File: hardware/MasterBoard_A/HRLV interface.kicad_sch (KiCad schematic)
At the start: 27 parts, among them Q10 MMBT5550L, Q11 MMBT5550L, Q3 MMBT5550L, U30 MCP2542FDxMF, U31 STISO620, U32 STISO620

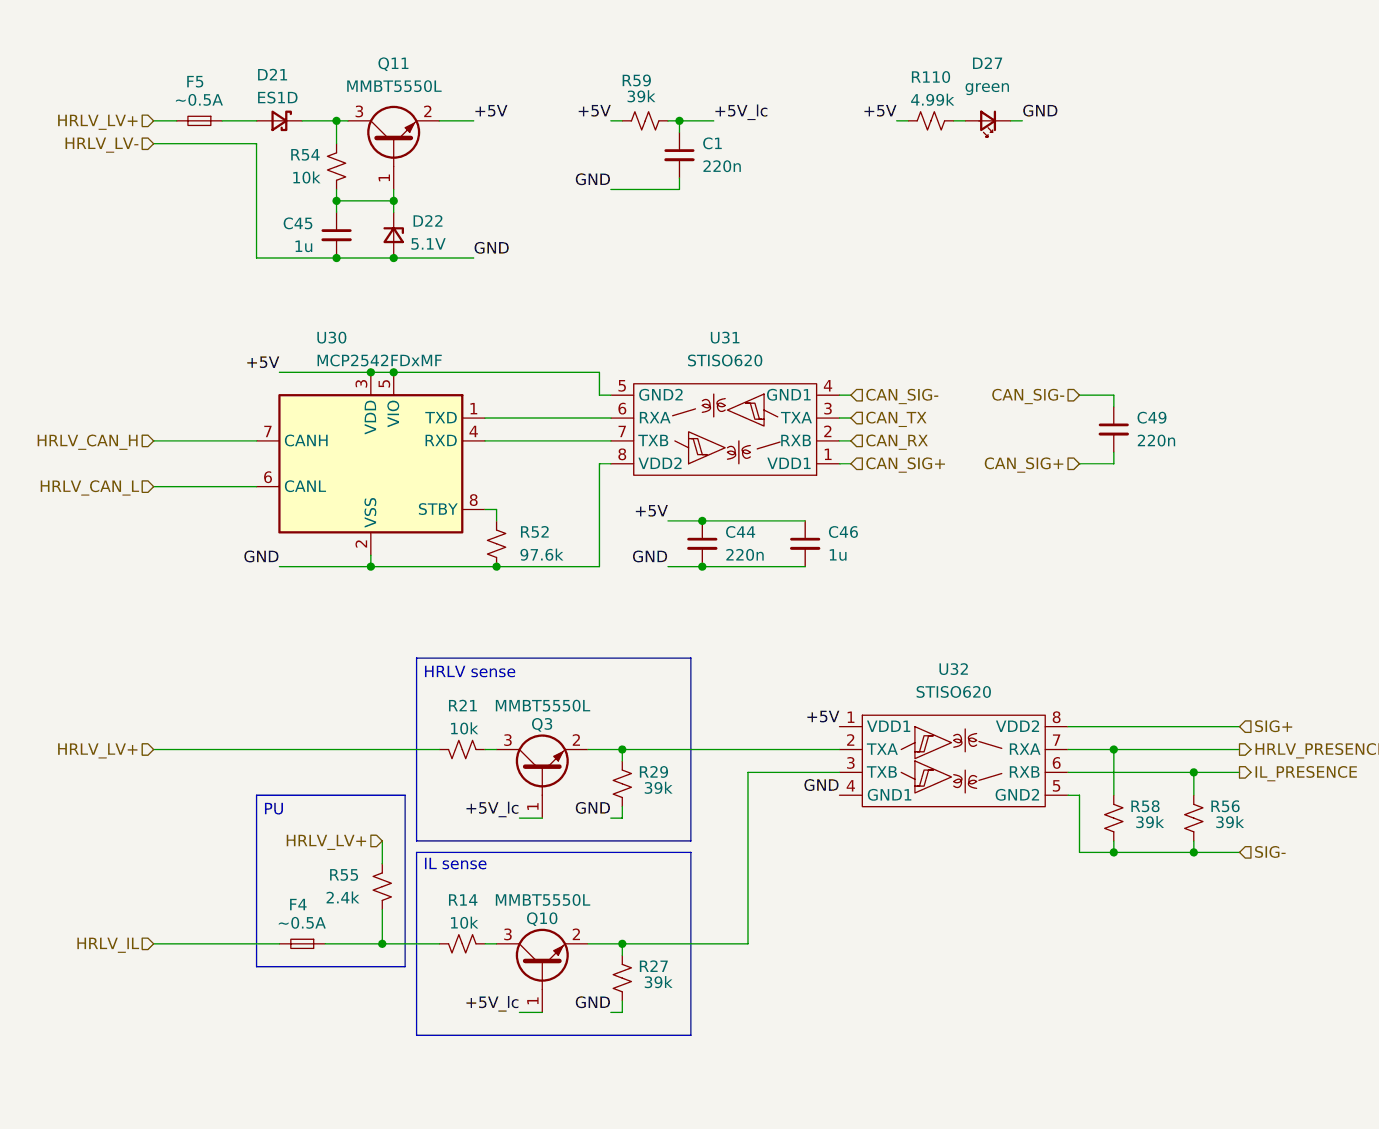
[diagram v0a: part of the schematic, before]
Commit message: better-ified power stuff. new costing program
handy new costing program for kicad. just c&p symbols directly from kicad into it and itll dump out the BOM cost of what ever you gave it
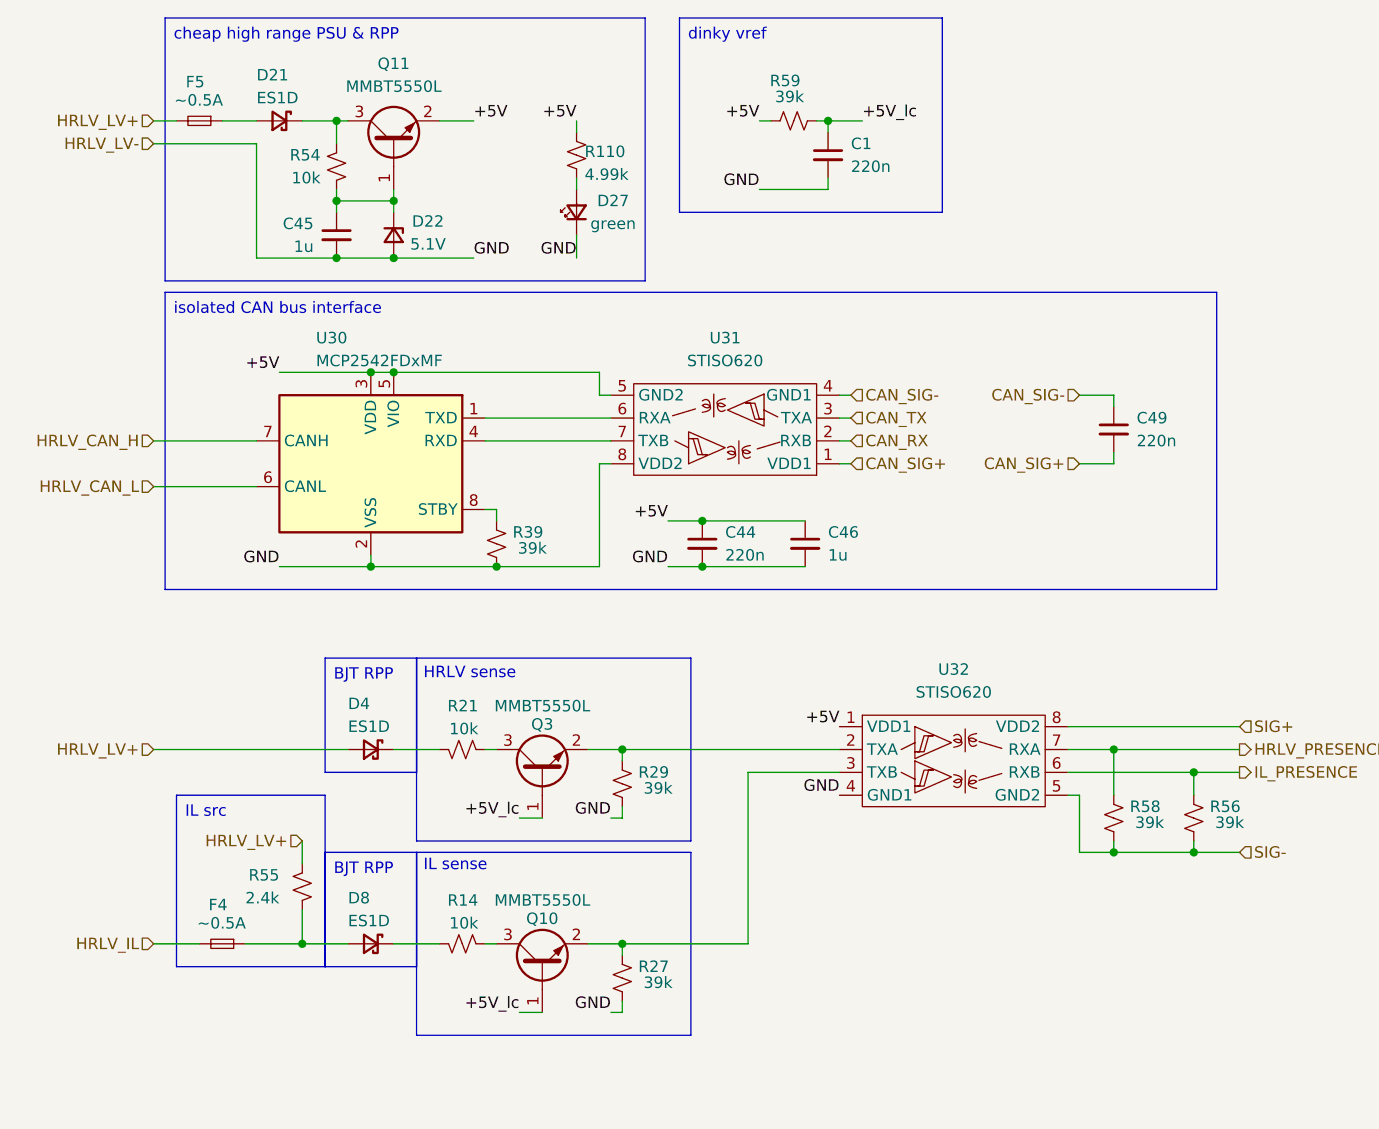
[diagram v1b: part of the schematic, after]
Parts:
- removed R52: 97.6k, Resistor_SMD:R_0805_2012Metric_Pad1.20x1.40mm_HandSolder, symbol Device:R_Small_US
- added D4, D8: ES1D, Diode_SMD:D_SMA, symbol Device:D_Schottky_Small
- added R39: 39k, Resistor_SMD:R_0805_2012Metric_Pad1.20x1.40mm_HandSolder, symbol Device:R_Small_US
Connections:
- net HRLV_LV+: now also D4.2 (A); no longer R21.1
- net HRLV_LV-: now also R39.1
- net at F4.1, R55.1: now also D8.2 (A); no longer R14.1
- net at U30.8 (STBY): now also R39.2
- new net: D4.1 (K), R21.1
- new net: D8.1 (K), R14.1
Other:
- note removed: "PU"
- moved on the sheet: C1, D27, F4, R110, R55, R59

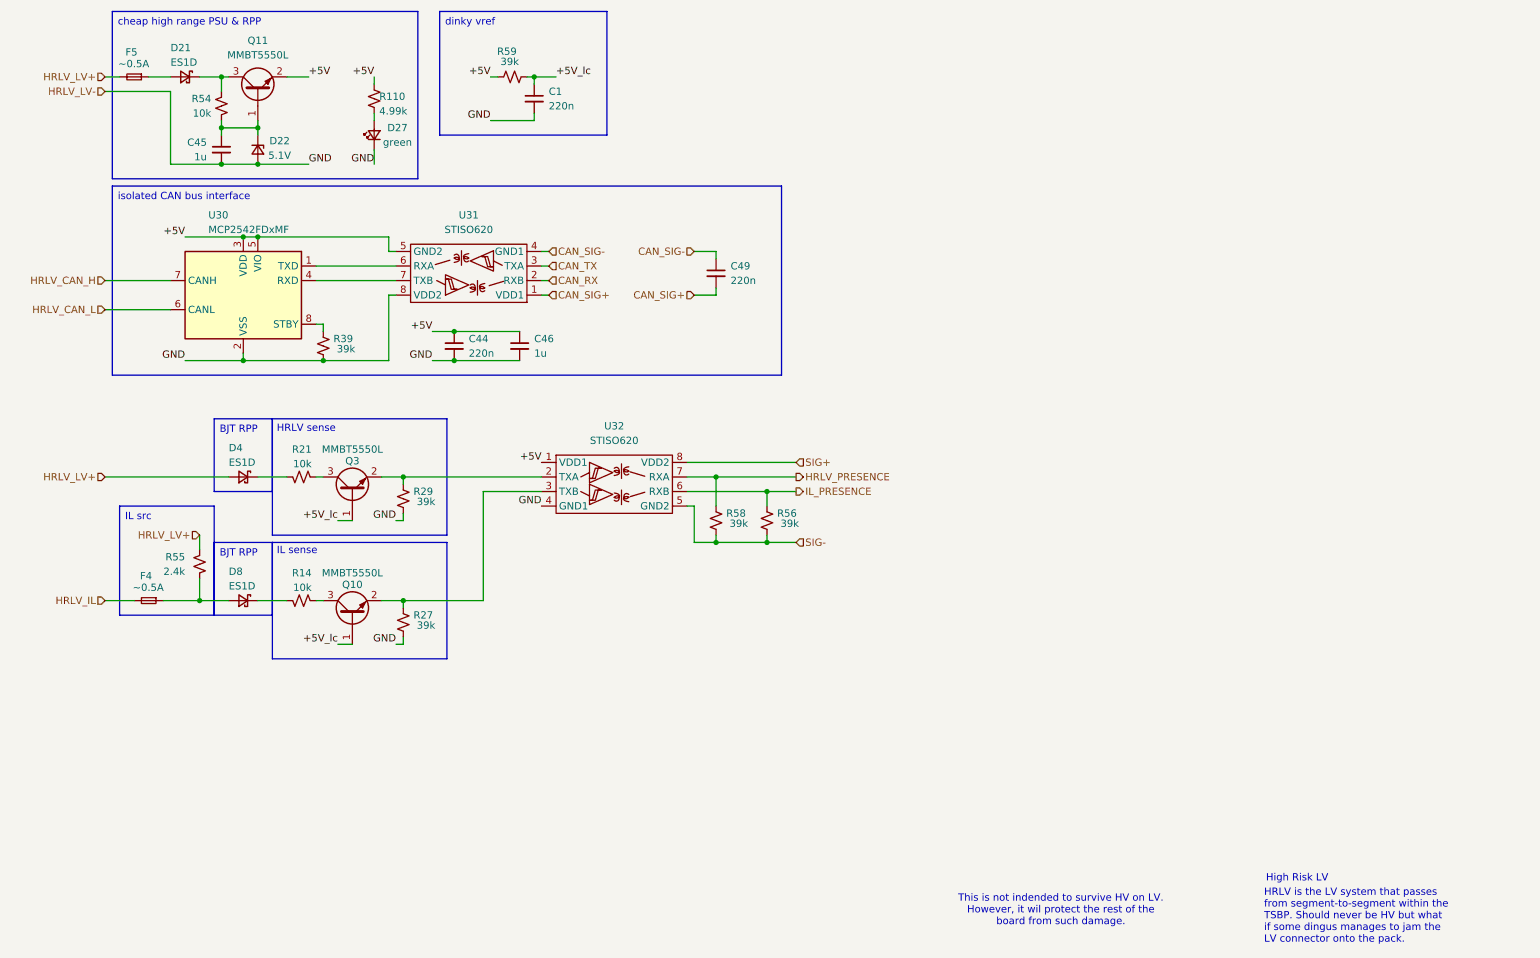
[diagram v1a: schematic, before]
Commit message: near final
missing direct MCU connections, pin map excel sheet needs piddled with. schematic needs reviewed
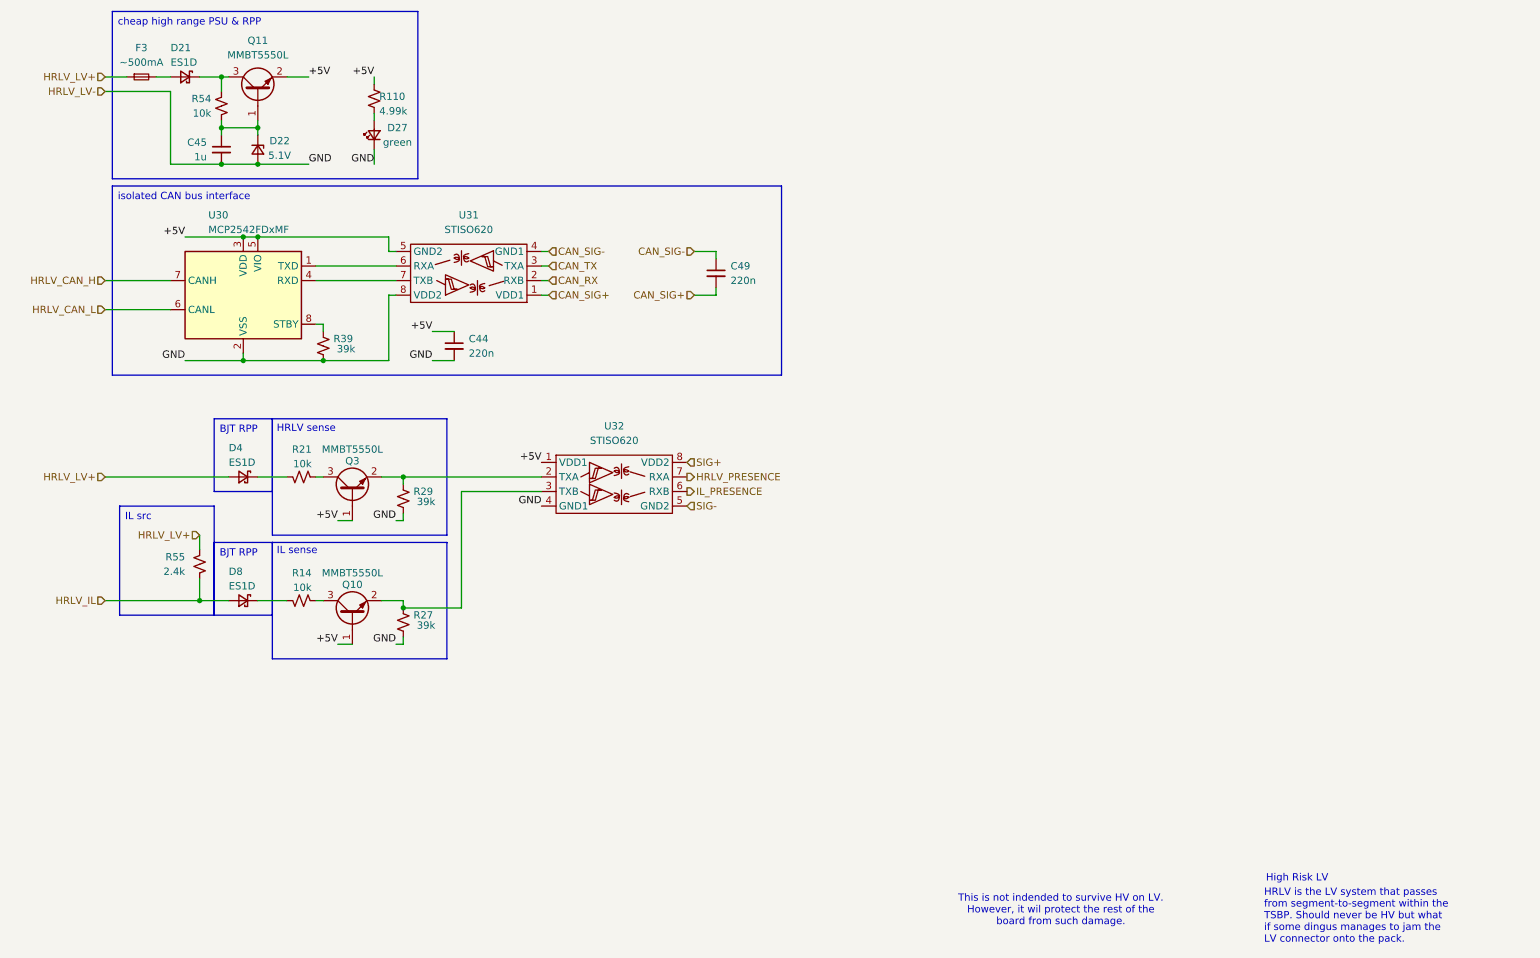
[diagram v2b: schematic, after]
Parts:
- removed C1: 220n, Capacitor_SMD:C_0805_2012Metric_Pad1.18x1.45mm_HandSolder, symbol Device:C_Small
- removed C46: 1u, Capacitor_SMD:C_1206_3216Metric_Pad1.33x1.80mm_HandSolder, symbol Device:C_Small
- removed F4, F5: ~0.5A, Resistor_THT:R_Box_L13.0mm_W4.0mm_P9.00mm, symbol Device:Fuse_Small
- removed R56, R58, R59: 39k, Resistor_SMD:R_0805_2012Metric_Pad1.20x1.40mm_HandSolder, symbol Device:R_Small_US
- added F3: ~500mA, Fuse:Fuseholder_Blade_Mini_Keystone_3568, symbol Device:Fuse_Small
- U32: footprint Package_SO:SOIC-8_5.3x6.2mm_P1.27mm -> Package_SO:PowerIntegrations_SO-8
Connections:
- net +5V_lc is gone; now on net +5V: Q10.1 (B), Q3.1 (B)
- net HRLV_IL: now also D8.2 (A), R55.1
- net HRLV_LV+: now also F3.1
- net at D21.2 (A): now also F3.2

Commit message: one must have hope
eyeballed the ethernet transmission lines, i think it'll work. absolute pain without using footprints smaller than 0805 but it think itll be fine. also shuffled together the PWM sig bank
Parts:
- U30: footprint Package_SO:JEITA_SOIC-8_3.9x4.9mm_P1.27mm -> Package_SO:SOIC-8_3.9x4.9mm_P1.27mm

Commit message: up to date meta sheet and made release files
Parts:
- C44, C49: unit x1 (none) -> 0.054
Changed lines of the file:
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@@
+			)
+		)
+		(property "unit x1" "0.054"
+			(at 138.43 62.23 0)
+			(effects
+				(font
+					(size 1.27 1.27)
+				)
+				(hide yes)
 			)
 		)
@@
 			(at 92.71 74.93 0)
 			(effects
+				(font
+					(size 1.27 1.27)
+				)
+				(hide yes)
+			)
+		)
+		(property "unit x1" "0.054"
+			(at 92.71 74.93 0)
+			(effects

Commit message: mb v1.1 on da way
shuffled around stuff. review notes. made notes. glory to those who look forward and all that fuzz
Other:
- company: (none) -> UTA Racing
- title: (none) -> BeeMS Master Board (A)
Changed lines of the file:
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@@
 	(generator_version "9.0")
 	(paper "A4")
+	(title_block
+		(title "BeeMS Master Board (A)")
+		(company "UTA Racing")
+		(comment 1 "Files at github.com/Gregification/BeeMS")
+	)
 	(rectangle
 		(start 60.96 109.22)

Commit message: mb 1.1 on da way. more shuffling
trying to be more professional about the part choices. obtuse excel sheet of pain has arrived.
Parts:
- removed C45: 1u, Capacitor_SMD:C_1206_3216Metric_Pad1.33x1.80mm_HandSolder, symbol Device:C_Small
- removed D21, D4, D8: ES1D, Diode_SMD:D_SMA, symbol Device:D_Schottky_Small
- removed D22: 5.1V, Diode_SMD:D_0805_2012Metric_Pad1.15x1.40mm_HandSolder, symbol Device:D_Zener_Small
- removed D27: green, LED_SMD:LED_0805_2012Metric_Pad1.15x1.40mm_HandSolder, symbol Device:LED_Small
- removed F3: ~500mA, Fuse:Fuseholder_Blade_Mini_Keystone_3568, symbol Device:Fuse_Small
- removed Q11, Q3: MMBT5550L, Package_TO_SOT_SMD:SOT-23, symbol Transistor_BJT:MMBT5550L
- removed R110: 4.99k, Resistor_SMD:R_1206_3216Metric_Pad1.30x1.75mm_HandSolder, symbol Device:R_Small_US
- removed R14, R21, R54: 10k, Resistor_SMD:R_0805_2012Metric_Pad1.20x1.40mm_HandSolder, symbol Device:R_Small_US
- removed R27, R29, R39: 39k, Resistor_SMD:R_0805_2012Metric_Pad1.20x1.40mm_HandSolder, symbol Device:R_Small_US
- removed R55: 2.4k, Resistor_SMD:R_0805_2012Metric_Pad1.20x1.40mm_HandSolder, symbol Device:R_Small_US
- removed U32: STISO620, Package_SO:PowerIntegrations_SO-8, symbol zzLocalLibrary:STISO620TR
- added C501, C505: 1u, Capacitor_SMD:C_1206_3216Metric_Pad1.33x1.80mm_HandSolder, symbol Device:C_Small
- added C502: 220n, Capacitor_SMD:C_0805_2012Metric_Pad1.18x1.45mm_HandSolder, symbol Device:C_Small
- added D501, D502: TS4148, Diode_SMD:D_0805_2012Metric_Pad1.15x1.40mm_HandSolder, symbol Device:D_Small
- added D503: ES1D, Diode_SMD:D_SMA, symbol Device:D_Schottky_Small
- added Q501: MMBT5550L, Package_TO_SOT_SMD:SOT-23, symbol Transistor_BJT:MMBT5550L
- added R501, R503, R505: 40.2k, Resistor_SMD:R_0805_2012Metric_Pad1.20x1.40mm_HandSolder, symbol Device:R_Small_US
- added R502, R504: 2.4k, Resistor_SMD:R_0805_2012Metric_Pad1.20x1.40mm_HandSolder, symbol Device:R_Small_US
- added R506: 4.7, Resistor_SMD:R_1206_3216Metric_Pad1.30x1.75mm_HandSolder, symbol Device:R_Small_US
- added U501: Si1450DH, Package_TO_SOT_SMD:SOT-363_SC-70-6, symbol zzLocalLibrary:Si1480DH
- added U502: AP7384-50SA, Package_TO_SOT_SMD:SOT-23, symbol Regulator_Linear:AP7384-50SA
- added U503: NCV68061, Package_TO_SOT_SMD:TSOT-23-6, symbol zzLocalLibrary:NCV68061
- added U506, U507: ISOM8110, zzLocalLibraries-Footprints:ISOM811_SOIC-4_DFG, symbol zzLocalLibrary:ISOM811_0_3
- added U508: NSI5030, Diode_SMD:Nexperia_CFP3_SOD-123W, symbol zzLocalLibrary:NSI45030
- renumbered C44 to C503, C49 to C504, Q10 to Q502, U31 to U504, U30 to U505
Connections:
- net +5V: now also U504.8 (VDD2), C501.1, Q501.1 (B), U502.2 (VO); no longer U504.5 (GND2)
- net CAN_SIG+: now also C504.1; no longer C504.2
- net CAN_SIG-: now also C504.2; no longer C504.1
- net HRLV_IL: now also D502.2 (A), R506.1
- net HRLV_LV+: now also U501.4 (S), U503.3 (EN), U503.6 (S)
- net HRLV_LV-: now also U504.5 (GND2), C501.2, C502.2, C505.2, R501.1, R502.1, R504.1, U502.3 (GND), U503.2 (GND); no longer U504.8 (VDD2)
- net HRLV_PRESENCE: now also R503.2, U506.3 (E)
- net IL_PRESENCE: now also R505.2, U507.3 (E)
- net at Q502.2 (E): now also U507.1 (+TX)
- net at Q502.3 (C): now also D502.1 (K)
- net at U505.8 (STBY): now also R501.2
- new net: U501.3 (G), U503.5 (G)
- new net: D503.2 (A), U508.1
- new net: C505.1, D503.1 (K), R506.2
- new net: Q501.2 (E), U506.1 (+TX)
- new net: D501.1 (K), Q501.3 (C)
- new net: R504.2, U507.2 (-TX)
- new net: R502.2, U506.2 (-TX)
- new net LV+: C502.1, D501.2 (A), U501.1 (D), U501.2 (D), U501.5 (D), U501.6 (D), U502.1 (VI), U503.4 (D), U508.2
- new net VDD: U506.4 (C), U507.4 (C)
- new net VSS: R503.1, R505.1
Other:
- note added: "This is not indended to survive HV. However, this will limit damage to this sheet"
- note removed: "HRLV sense"
- note removed: "IL sense"
- note removed: "This is not indended to survive HV on LV. However, it wil protect the rest of the board from such damage."
- moved on the sheet: C503, C504, Q502, U504, U505

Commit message: excel monkey has monkey do-ne it
eyeballed a format for the psu table, it gets the point across
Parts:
- removed D503: ES1D, Diode_SMD:D_SMA, symbol Device:D_Schottky_Small
- removed R503: 40.2k, Resistor_SMD:R_0805_2012Metric_Pad1.20x1.40mm_HandSolder, symbol Device:R_Small_US
- removed R506: 4.7, Resistor_SMD:R_1206_3216Metric_Pad1.30x1.75mm_HandSolder, symbol Device:R_Small_US
- added C501: 220n, Capacitor_SMD:C_0805_2012Metric_Pad1.18x1.45mm_HandSolder, symbol Device:C_Small
- added D503: TS4148, Diode_SMD:D_0805_2012Metric_Pad1.15x1.40mm_HandSolder, symbol Device:D_Small
- added D504: 10V, Diode_SMD:D_0805_2012Metric_Pad1.15x1.40mm_HandSolder, symbol Device:D_Zener_Small
- added R501: 88.7k, Resistor_SMD:R_0805_2012Metric_Pad1.20x1.40mm_HandSolder, symbol Device:R_Small_US
- added R508: 2.4k, Resistor_SMD:R_0805_2012Metric_Pad1.20x1.40mm_HandSolder, symbol Device:R_Small_US
- R505: value 40.2k -> 100; footprint Resistor_SMD:R_0805_2012Metric_Pad1.20x1.40mm_HandSolder -> Resistor_SMD:R_1206_3216Metric_Pad1.30x1.75mm_HandSolder; mouser https://www.mouser.com/ProductDetail/KOA-Speer/RK73H2ATTD40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 -> https://www.mouser.com/ProductDetail/ROHM-Semiconductor/ESR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; specs 40.2k ohm, 250mW, 1%, 150V, 100ppm, -55C, +155C -> 100 omh, thick, anti surge, 1%, 750mW, 200V, -55C, +155C, 1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; unit x1 0.1 -> 0.17; unit x10 0.02 -> 0.055
- renumbered C505 to C502, C501 to C503, C502 to C504, C503 to C505, C504 to C506, R504 to R502, R502 to R503, R501 to R504, U508 to U501, U501 to U502, U505 to U504, U502 to U505, U504 to U508
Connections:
- net HRLV_IL is gone; now on net LV+: D502.2 (A)
- net VSS is gone; now on an unnamed net: R505.1
- net HRLV_LV-: now also C501.2, R501.1, R508.1; no longer R502.1
- net IL_PRESENCE: no longer R505.2
- net LV+: no longer D501.2 (A)
- net at U501.1: now also D503.2 (A)
- net at C502.1: now also D503.1 (K)
- net at D501.1 (K): now also R502.2, R501.2; no longer Q501.3 (C)
- net at U507.2 (-TX): now also R508.2; no longer R502.2
- net at D502.1 (K): now also Q501.3 (C); no longer Q502.3 (C)
- new net: C501.1, D504.1 (K), R502.1
- new net: D504.2 (A), Q502.3 (C)
- new net HRLV_IL+: R505.2
- new net HRLV_IL-: D501.2 (A)
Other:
- moved on the sheet: Q502, R502, U507

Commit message: multi channel propaganda
only bots use multi channel layouts
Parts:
- renumbered R508 to R506
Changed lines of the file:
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@@
 		(on_board yes)
 		(dnp no)
-		(property "Reference" "R508"
+		(property "Reference" "R506"
 			(at 69.215 145.161 0)
 			(effects
@@
 			(project "MasterBoard_A"
 				(path "/20ac6af0-79b5-4ba6-aad3-75081d02c913/258b64a8-9b08-463b-aff1-8236af04e061"
-					(reference "R508")
+					(reference "R506")
 					(unit 1)
 				)
